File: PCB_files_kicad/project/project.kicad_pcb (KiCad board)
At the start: 2 copper layers, 100 x 100 mm, 42 parts, among them J1 Conn_01x08_Female, J2 S1, J3 S2, J4 Conn_01x08_Female, J5 Display, J6 HC06, J7 Barrel_Jack, J8 USB_B_Micro, Q1 IRF7240PBF, U1 24AA64FT-I/OT, U2 TP4056, U3 MT3608, U4 BluePill_Connector

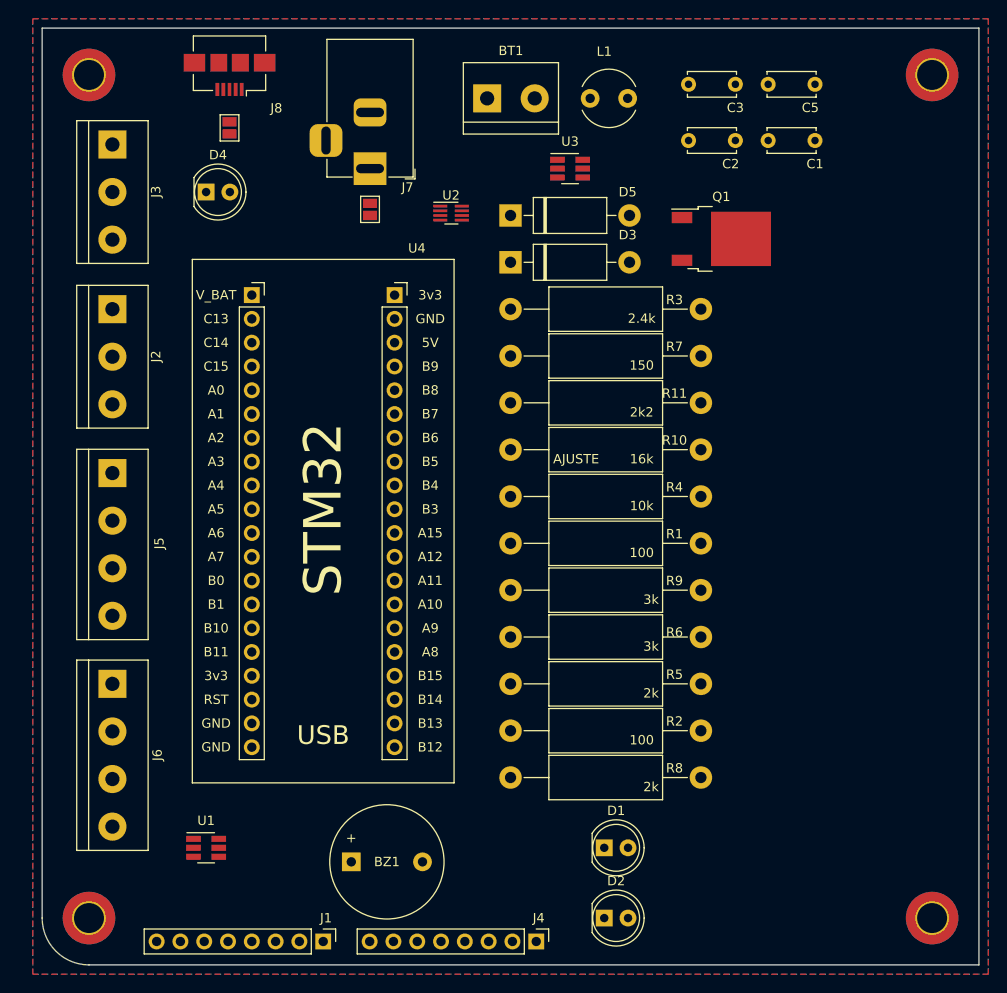
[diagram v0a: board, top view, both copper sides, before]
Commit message: PCB - Starting to route
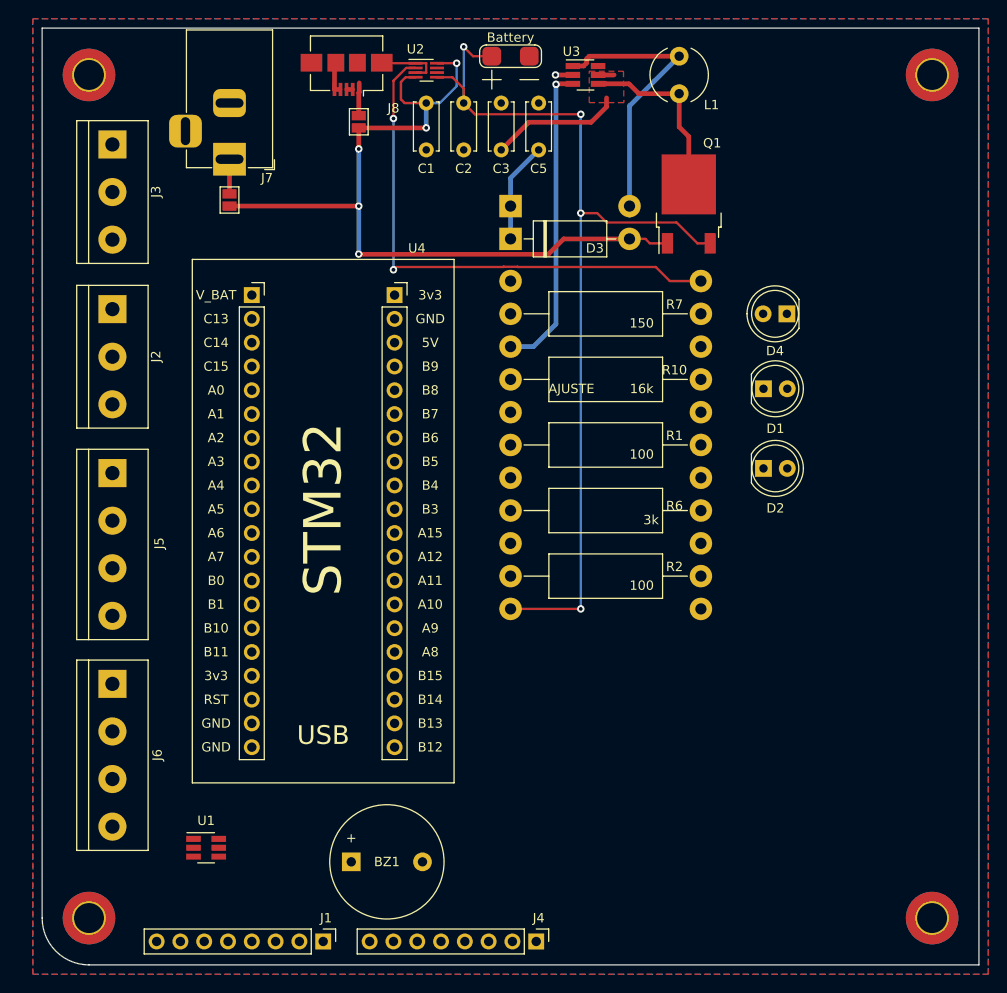
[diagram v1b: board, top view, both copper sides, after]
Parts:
- Battery: renamed from BT1; footprint TerminalBlock:TerminalBlock_bornier-2_P5.08mm -> mylib:Batt
- D5, R11, R3, R4, R5, R8, R9: moved to B.Cu
- moved D4 63.3 mm to (174.5, 80.5), turned to 180 degrees
- moved D1 51.9 mm to (172.0, 88.5)
- moved D2 50.9 mm to (172.0, 97.0)
- moved C1 36.7 mm to (136.0, 58.0), turned to 270 degrees
- moved C5 25.5 mm to (148.0, 63.0), turned to 90 degrees
- moved C2 24.3 mm to (140.0, 58.0), turned to 270 degrees
- moved C3 21.2 mm to (144.0, 63.0), turned to 90 degrees
- moved R8 18.0 mm to (145.0, 112.0)
- moved R2 16.5 mm to (145.0, 108.5)
- moved U2 15.5 mm to (136.0, 54.5)
- moved J7 15.0 mm to (115.0, 64.0)
- moved JP1 15.0 mm to (115.0, 68.3)
- moved R5 15.0 mm to (145.0, 105.0)
- moved JP2 13.8 mm to (128.8, 60.0)
- moved R6 13.5 mm to (145.0, 101.5)
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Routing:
- net /BATT: track 0.00 -> 112.7 mm, vias 0 -> 4
- net /MEASURE: track 0.00 -> 86.2 mm, vias 0 -> 5
- net Net-(R3-Pad2): track 0.00 -> 56.7 mm, vias 0 -> 2
- net Net-(C3-Pad1): track 0.00 -> 35.0 mm
- net Net-(R10-Pad2): track 0.00 -> 33.3 mm, vias 0 -> 1
- net Net-(D5-Pad2): track 0.00 -> 31.2 mm
- net Earth: track 0.00 -> 12.3 mm, vias 0 -> 1
- net +5V: track 0.00 -> 10.7 mm
- net Net-(J7-Pad1): track 0.00 -> 3.70 mm
- net Net-(J8-Pad1): track 0.00 -> 3.52 mm
- net Net-(J8-Pad2): track 0.00 -> 0.65 mm
- added copper zone on F.Cu, net Net-(C3-Pad1)

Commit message: PCB v1.0 done
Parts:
- moved D4 57.3 mm to (162.5, 136.5), turned to 0 degrees
- moved D1 41.1 mm to (162.5, 128.5)
- moved H1 25.0 mm to (165.0, 55.0)
- moved H3 25.0 mm to (165.0, 145.0)
- moved D2 24.9 mm to (162.5, 120.0)
- moved L1 11.3 mm to (155.0, 65.0)
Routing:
- net +5V: track 10.7 -> 218.8 mm, vias 0 -> 3
- net +3V3: track 0.00 -> 159.6 mm, vias 0 -> 7
- net /I2C1_SDA: track 0.00 -> 113.8 mm, vias 0 -> 5
- net /I2C1_SCL: track 0.00 -> 103.2 mm, vias 0 -> 5
- net /blupill/SENSOR2_GPIO: track 0.00 -> 77.4 mm, vias 0 -> 2
- net /blupill/ADC12_IN1: track 0.00 -> 69.5 mm, vias 0 -> 3
- net /UART1_RX: track 0.00 -> 67.6 mm, vias 0 -> 1
- net /blupill/LED1_GPIO: track 0.00 -> 67.1 mm, vias 0 -> 2
- net /UART1_TX: track 0.00 -> 65.7 mm, vias 0 -> 2
- net /blupill/L1_GPIO: track 0.00 -> 65.1 mm, vias 0 -> 1
- net /blupill/C1_GPIO: track 0.00 -> 64.3 mm, vias 0 -> 1
- net /blupill/ADC12_IN0: track 0.00 -> 60.9 mm, vias 0 -> 1
- net Net-(D4-Pad2): track 0.00 -> 60.8 mm
- net /blupill/L2_GPIO: track 0.00 -> 60.7 mm, vias 0 -> 1
- net /blupill/C2_GPIO: track 0.00 -> 58.2 mm, vias 0 -> 1
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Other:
- board size 100 x 100 mm -> 75 x 100 mm
- board text added: "+3V3"
- board text added: "+5V"
- board text added: "GND"
- board text added: "IR-A8"
- board text added: "IR-A9"
- board text added: "LED 1"
- board text added: "LED 2"
- board text added: "Power ON"

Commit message: SCH version 1.3
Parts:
- added R12: 2k2, Resistor_THT:R_Axial_DIN0414_L11.9mm_D4.5mm_P20.32mm_Horizontal, F.Cu at (145.0, 115.5)
- added R13: 2k2, Resistor_THT:R_Axial_DIN0414_L11.9mm_D4.5mm_P20.32mm_Horizontal, B.Cu at (145.0, 119.0)
- added TP1: PowerSupply, TestPoint:TestPoint_THTPad_D2.0mm_Drill1.0mm, F.Cu at (138.0, 68.0)
- added TP2: Batt, TestPoint:TestPoint_THTPad_D2.0mm_Drill1.0mm, F.Cu at (133.0, 68.0)
- added TP3: Qdrain, TestPoint:TestPoint_THTPad_D2.0mm_Drill1.0mm, F.Cu at (128.0, 68.0)
- added TP4: out5v, TestPoint:TestPoint_THTPad_D2.0mm_Drill1.0mm, F.Cu at (123.0, 68.0)
- Q1: value IRF7240PBF -> Irf9z20; footprint Package_TO_SOT_SMD:TO-252-2 -> Package_TO_SOT_THT:TO-220-3_Vertical
- moved D2 27.5 mm to (155.0, 146.5)
- moved D1 11.7 mm to (155.0, 137.5)
- moved D4 10.6 mm to (155.0, 129.0)
- moved BZ1 8.87 mm to (136.2, 142.2), turned to 90 degrees
- moved Q1 4.94 mm to (162.8, 64.0), turned to 270 degrees
- renumbered Battery to BT1
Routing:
- net /I2C1_SDA: track 113.8 -> 174.8 mm, vias 5 -> 7
- net /I2C1_SCL: track 103.2 -> 136.6 mm
- net +5V: track 218.8 -> 249.5 mm, vias 3 -> 5
- net Net-(D2-Pad2): track 12.9 -> 41.2 mm
- net Net-(C3-Pad1): track 42.2 -> 63.1 mm
- net Net-(D1-Pad2): track 35.5 -> 53.5 mm, vias 0 -> 1
- net /blupill/LED2_GPIO: track 48.6 -> 65.1 mm, vias 0 -> 2
- net /MEASURE: track 137.8 -> 153.7 mm
- net /Buzzer: track 37.8 -> 49.6 mm, vias 1 -> 2
- net /BATT: track 114.2 -> 122.5 mm
- net /blupill/C1_GPIO: track 64.3 -> 62.6 mm
- net /blupill/LED1_GPIO: track 67.1 -> 68.6 mm
- net Net-(R3-Pad2): track 56.7 -> 58.1 mm
- net /blupill/ADC12_IN0: track 60.9 -> 59.5 mm
- net Net-(D4-Pad2): vias 0 -> 1
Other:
- board text added: "Power"
- board text added: "RX"
- board text added: "SCL"
- board text added: "SDA"
- board text added: "TX"
- board text removed: "Power ON"

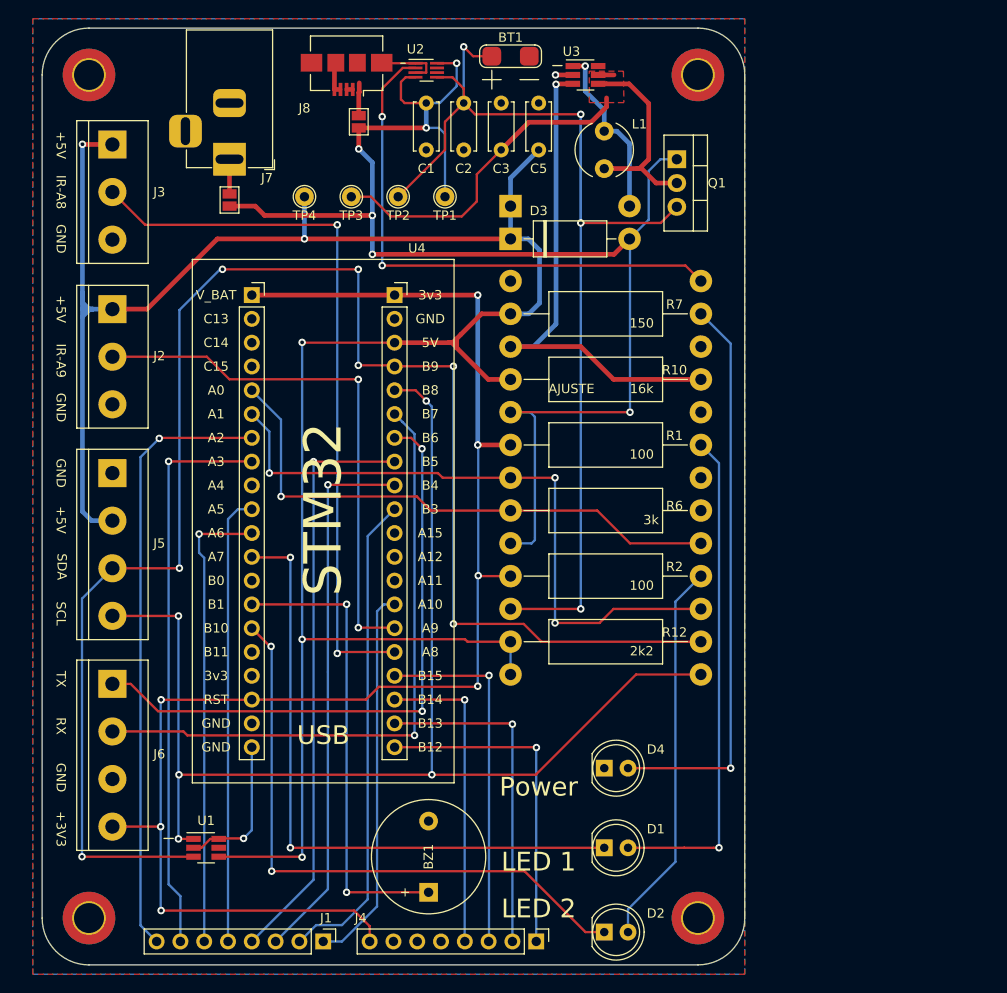
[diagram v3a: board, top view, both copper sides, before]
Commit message: Lot of changes.. BOM was added and UTN logo too
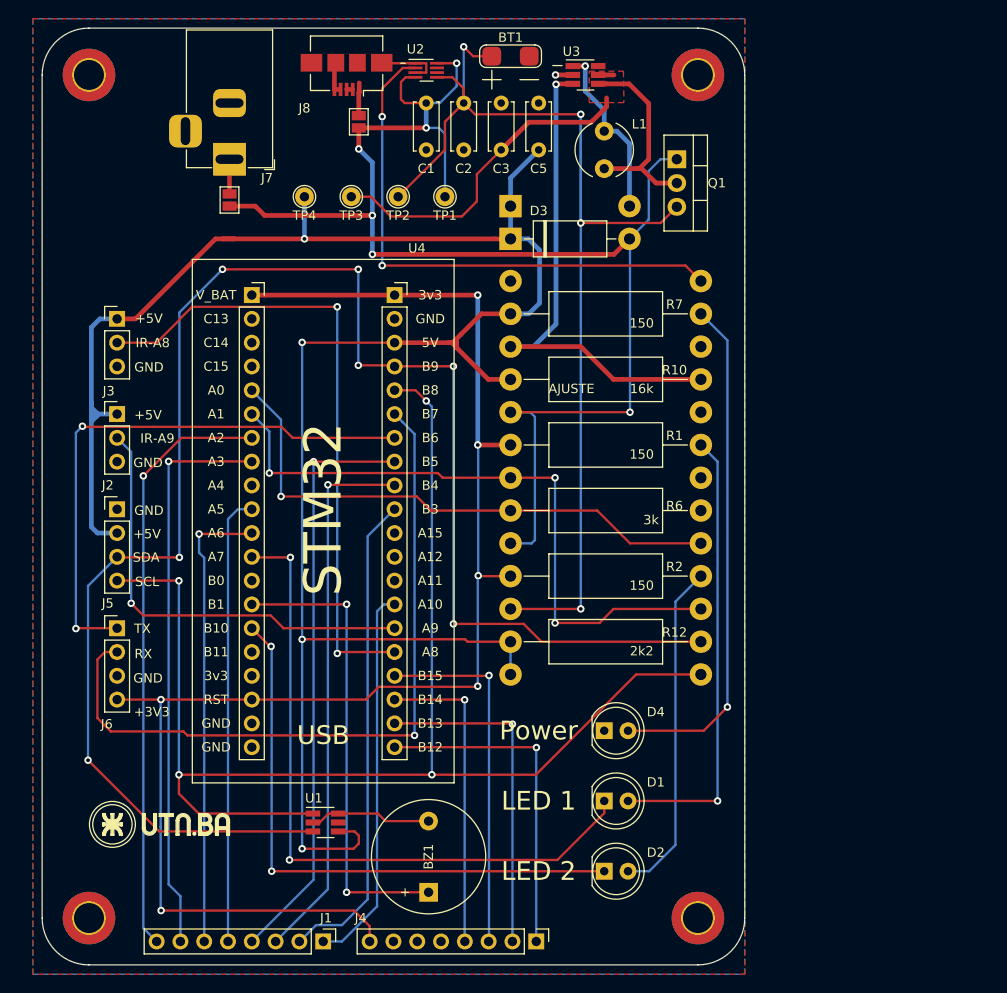
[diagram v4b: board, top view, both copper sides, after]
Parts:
- added LogoUTN.BA-Letras: UTN.BA-Letras, mylib:UTN.BA-Letras, F.Cu at (102.5, 135.0)
- C3: value 22uF-X5R -> 22uF
- J2, J3: footprint TerminalBlock:TerminalBlock_bornier-3_P5.08mm -> Connector_PinHeader_2.54mm:PinHeader_1x03_P2.54mm_Vertical
- J5, J6: footprint TerminalBlock:TerminalBlock_bornier-4_P5.08mm -> Connector_PinHeader_2.54mm:PinHeader_1x04_P2.54mm_Vertical
- Q1: value Irf9z20 -> IRF9Z20
- R1, R2: value 100 -> 150
- moved J3 18.6 mm to (103.0, 81.0), turned to 0 degrees
- moved U1 13.0 mm to (125.2, 134.8)
- moved J2 11.2 mm to (103.0, 91.2), turned to 0 degrees
- moved D2 6.50 mm to (155.0, 140.0)
- moved J6 5.96 mm to (103.0, 114.1), turned to 0 degrees
- moved D1 5.00 mm to (155.0, 132.5)
- moved D4 4.00 mm to (155.0, 125.0)
- moved J5 3.89 mm to (103.0, 101.4), turned to 0 degrees
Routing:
- net +5V: track 249.5 -> 230.1 mm, vias 5 -> 4
- net /I2C1_SCL: track 136.6 -> 148.7 mm, vias 5 -> 4
- net /UART1_RX: track 67.6 -> 78.5 mm
- net /blupill/SENSOR1_GPIO: track 57.6 -> 47.5 mm, vias 2 -> 1
- net /blupill/SENSOR2_GPIO: track 77.4 -> 68.3 mm
- net Net-(D4-Pad2): track 60.8 -> 54.8 mm
- net /UART1_TX: track 65.7 -> 60.1 mm
- net Net-(D1-Pad2): track 53.5 -> 48.3 mm
- net Net-(D2-Pad2): track 41.2 -> 36.0 mm
- net /blupill/LED1_GPIO: track 68.6 -> 73.5 mm
- net /I2C1_SDA: track 174.8 -> 179.1 mm
- net Earth: track 28.2 -> 25.4 mm, vias 2 -> 1
- net /blupill/LED2_GPIO: track 65.1 -> 62.4 mm
- net /blupill/L1_GPIO: track 65.1 -> 63.5 mm
- net +3V3: track 159.6 -> 159.1 mm, vias 7 -> 6

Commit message: Sche rev 1.4 - PCB rev 1.2
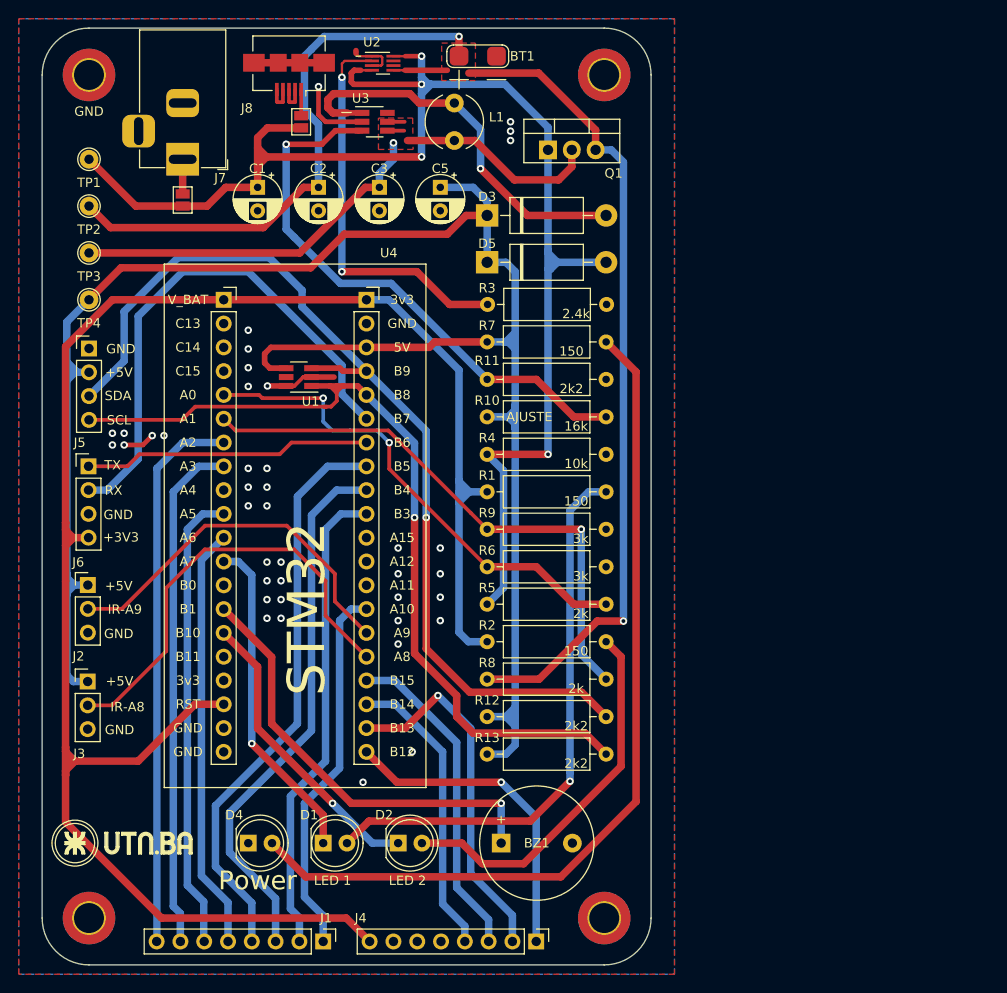
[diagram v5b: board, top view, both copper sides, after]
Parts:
- C1, C2, C3, C5: footprint Capacitor_THT:C_Disc_D5.0mm_W2.5mm_P5.00mm -> Capacitor_THT:CP_Radial_D5.0mm_P2.50mm
- D5: moved to F.Cu
- R1, R10, R12, R2, R6, R7: footprint Resistor_THT:R_Axial_DIN0414_L11.9mm_D4.5mm_P20.32mm_Horizontal -> Resistor_THT:R_Axial_DIN0309_L9.0mm_D3.2mm_P12.70mm_Horizontal
- R11, R13, R3, R4, R5, R8, R9: footprint Resistor_THT:R_Axial_DIN0414_L11.9mm_D4.5mm_P20.32mm_Horizontal -> Resistor_THT:R_Axial_DIN0309_L9.0mm_D3.2mm_P12.70mm_Horizontal; moved to F.Cu
- moved U1 47.6 mm to (122.4, 87.2), turned to 180 degrees
- moved D4 39.8 mm to (117.0, 137.0)
- moved J3 38.8 mm to (99.9, 119.8)
- moved TP1 38.2 mm to (100.0, 64.0), turned to 270 degrees
- moved TP2 33.0 mm to (100.0, 69.0), turned to 270 degrees
- moved D1 30.3 mm to (125.0, 137.0)
- moved TP3 28.6 mm to (100.0, 74.0), turned to 270 degrees
- moved TP4 25.5 mm to (100.0, 79.0), turned to 270 degrees
- moved U3 23.0 mm to (130.5, 60.0)
- moved D2 22.2 mm to (133.0, 137.0)
- moved C1 20.1 mm to (118.0, 67.0)
- moved J2 18.5 mm to (99.9, 109.5)
- moved C2 17.9 mm to (124.5, 67.0)
- moved J6 17.6 mm to (99.9, 96.8)
- moved J5 17.4 mm to (100.0, 84.2)
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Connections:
- U4 pad 19: /blupill/L4_GPIO -> /blupill/L3_GPIO
- U4 pad 21: /blupill/L3_GPIO -> /blupill/L4_GPIO
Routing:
- net /I2C1_SDA: track 179.1 -> 105.4 mm, vias 7 -> 1
- net /I2C1_SCL: track 148.7 -> 93.3 mm, vias 4 -> 1
- net +3V3: track 159.1 -> 200.5 mm, vias 6 -> 0
- net Net-(D4-Pad2): track 54.8 -> 94.1 mm, vias 1 -> 0
- net /blupill/LED1_GPIO: track 73.5 -> 35.4 mm, vias 2 -> 1
- net /BATT: track 122.5 -> 154.9 mm, vias 4 -> 2
- net /blupill/LED2_GPIO: track 62.4 -> 31.8 mm, vias 2 -> 1
- net /UART1_TX: track 60.1 -> 30.7 mm, vias 2 -> 0
- net Net-(D5-Pad2): track 19.0 -> 42.6 mm
- net /UART1_RX: track 78.5 -> 56.6 mm, vias 1 -> 0
- net /blupill/SENSOR2_GPIO: track 68.3 -> 47.5 mm, vias 2 -> 0
- net +5V: track 230.1 -> 214.4 mm, vias 4 -> 0
- net Net-(R3-Pad2): track 58.1 -> 42.5 mm
- net Net-(D1-Pad2): track 48.3 -> 60.1 mm
- net Earth: track 25.4 -> 34.9 mm, vias 1 -> 40
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- added copper zone on F.Cu, net /BATT
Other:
- board size 75 x 100 mm -> 65 x 100 mm

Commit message: Schematic v1.5 - PCB v1.3
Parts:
- added +3V3: TestPoint, TestPoint:TestPoint_THTPad_D2.0mm_Drill1.0mm, F.Cu at (100.0, 75.0)
- added REF**: OSHW-Logo2_9.8x8mm_SilkScreen, Symbol:OSHW-Logo2_9.8x8mm_SilkScreen, F.Cu at (123.0, 83.5)
- BZ1: footprint Buzzer_Beeper:Buzzer_12x9.5RM7.6 -> mylib:Batt
- D3: value CDBU0130L - 350mV -> 1N5822 - 500mV; footprint Diode_THT:D_DO-15_P12.70mm_Horizontal -> Diode_THT:D_DO-201AD_P15.24mm_Horizontal
- D5: value SS34 -> 1N5822 - 500mV; footprint Diode_THT:D_DO-15_P12.70mm_Horizontal -> Diode_THT:D_DO-201AD_P15.24mm_Horizontal
- R10: value 16k -> 15k
- R3: value 2.4k -> 2k2
- R5, R8: value 2k -> 2k2
- R6, R9: value 3k -> 3k3
- U1: value 24AA64FT-I/OT -> M24C02; footprint Package_TO_SOT_SMD:SOT-23-6_Handsoldering -> Package_DIP:DIP-8_W7.62mm
- moved U1 50.5 mm to (144.0, 132.9), turned to 0 degrees
- moved BZ1 43.0 mm to (101.5, 130.8), turned to 180 degrees
- moved BATT 4.00 mm to (100.0, 65.0)
- moved Qdrain 4.00 mm to (100.0, 70.0)
- moved Vin 4.00 mm to (100.0, 60.0)
- moved C5 2.50 mm to (135.0, 67.0)
- moved D5 2.50 mm to (141.0, 68.0)
- moved C3 2.00 mm to (129.0, 67.0)
- moved D3 1.80 mm to (141.0, 74.0)
- moved C2 1.50 mm to (123.0, 67.0)
- moved J1 1.50 mm to (125.0, 146.0)
- moved J4 1.50 mm to (147.7, 146.0)
- moved LogoUTN.BA-Letras 1.41 mm to (99.5, 136.0)
- moved +5V 1.00 mm to (100.0, 80.0)
- moved C1 1.00 mm to (117.0, 67.0)
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- renumbered TP4 to +5V, TP2 to BATT, TP3 to Qdrain, TP1 to Vin
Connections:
- U1 pad 1: /I2C1_SCL -> Earth
- U1 pad 3: /I2C1_SDA -> Earth
- U1 pad 4: +5V -> Earth
- U1 pad 5: Net-(U1-Pad5) -> /I2C1_SDA
- U1 pad 6: Earth -> /I2C1_SCL
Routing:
- net /Buzzer: track 46.6 -> 32.3 mm, vias 1 -> 2
- net /I2C1_SDA: track 105.4 -> 119.5 mm
- net +3V3: track 200.5 -> 213.8 mm
- net Earth: track 34.9 -> 27.5 mm, vias 40 -> 39
- net /I2C1_SCL: track 93.3 -> 98.6 mm
- net Net-(D4-Pad2): track 94.1 -> 98.0 mm
- net Net-(C3-Pad1): track 64.6 -> 67.9 mm
- net /MEASURE: track 159.8 -> 162.9 mm
- net Net-(D1-Pad2): track 60.1 -> 58.2 mm, vias 1 -> 2
- net /blupill/SPI2_SCK: track 38.6 -> 37.1 mm
- net /blupill/L2_GPIO: track 54.8 -> 53.3 mm
- net /blupill/C3_GPIO: track 51.0 -> 49.5 mm
- net /blupill/SPI2_MOSI: track 35.0 -> 33.5 mm
- net /blupill/SPI2_MISO: track 31.5 -> 30.0 mm
- net /blupill/L1_GPIO: track 58.8 -> 57.3 mm
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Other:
- board text added: "Fecha: 26/09/2021"
- board text added: "ON"
- board text added: "Rev:"
- board text added: "Técnicas Digitales II"
- board text removed: "Power"
